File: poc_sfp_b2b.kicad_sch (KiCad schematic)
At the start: 16 parts

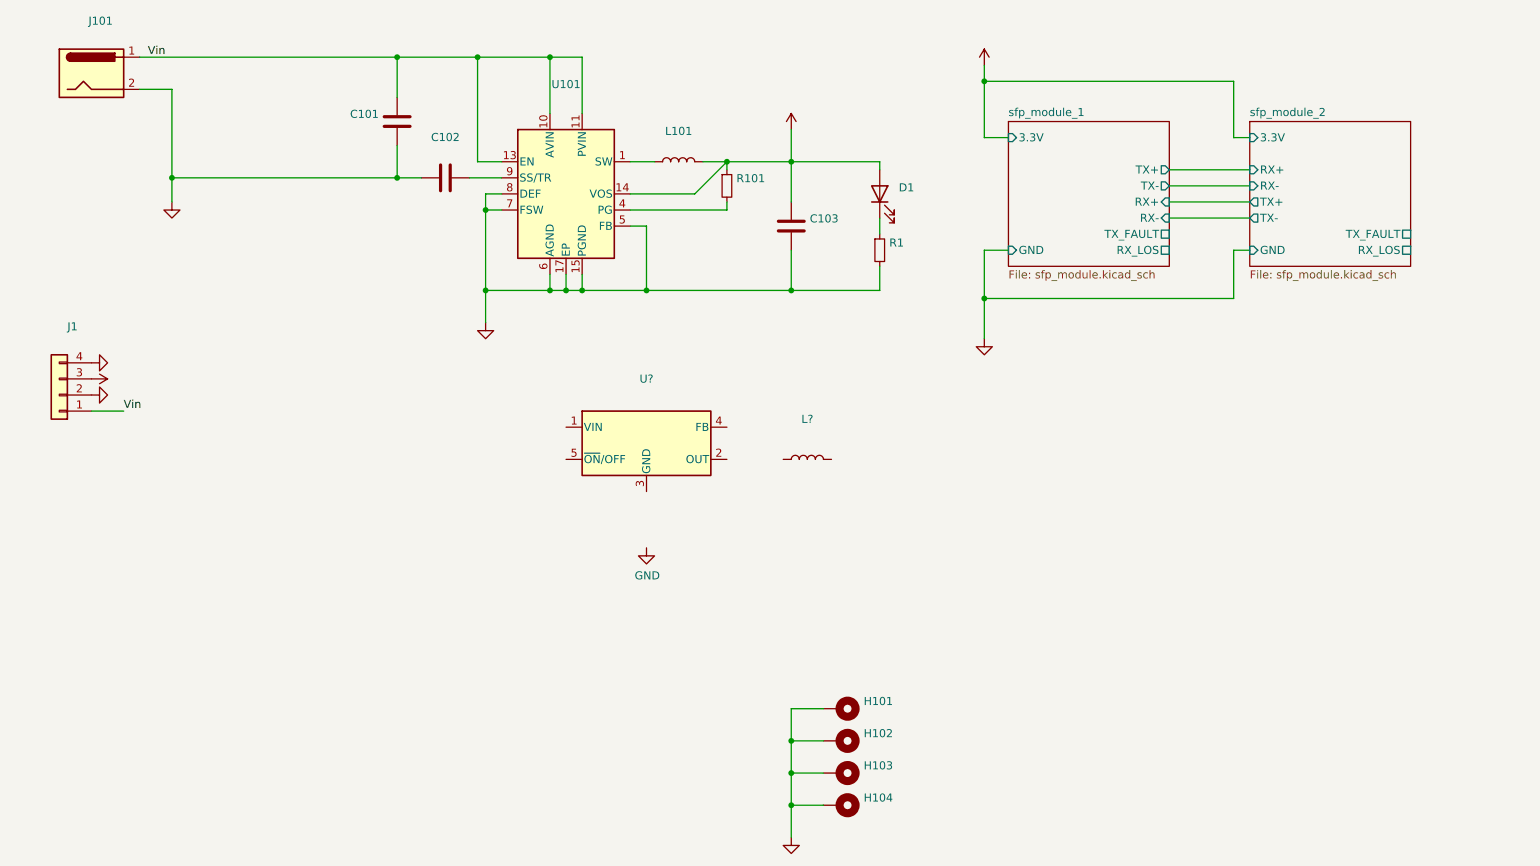
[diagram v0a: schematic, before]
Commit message: Replaced Mouser with LCSC Components
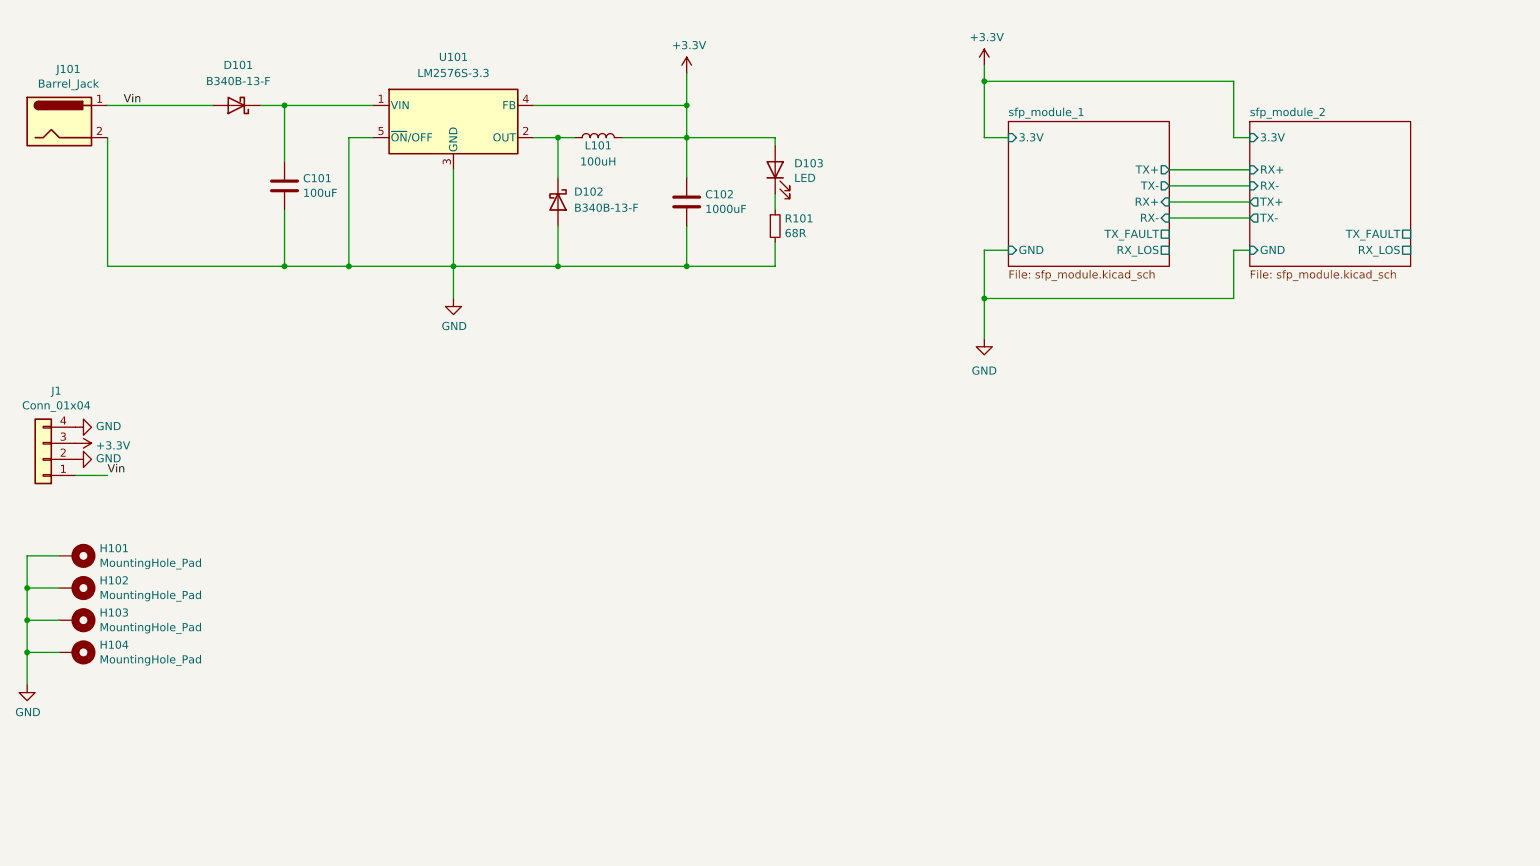
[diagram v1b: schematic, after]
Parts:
- removed C102: (no value), symbol Device:C
- removed L101: (no value), symbol Device:L
- removed R101: (no value), symbol Device:R_Small
- removed U101: (no value), symbol Regulator_Switching:TPS62142
- added D101, D102: B340B-13-F, Diode_SMD:D_SMB, symbol Device:D_Schottky
- C101: value (none) -> 100uF; footprint (none) -> Capacitor_SMD:CP_Elec_10x10; LCSC (none) -> C249838; Mouser Link https://www.mouser.de/ProductDetail/Samsung-Electro-Mechani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 -> (none); Mouser Part Number 187-CL32A106KAULNNE -> (none); Part Number CL32A106KAULNNE -> (none)
- C102: renamed from C103; value (none) -> 1000uF; footprint (none) -> Capacitor_SMD:CP_Elec_10x10; LCSC Part Number (none) -> C249844; Mouser Link https://www.mouser.de/ProductDetail/Samsung-Electro-Mechani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 -> (none); Mouser Part Number 187-CL21A226KQCLRNC -> (none); Part Number CL21A226KQCLRNC -> (none)
- D103: renamed from D1; value (none) -> LED; footprint (none) -> LED_THT:LED_D3.0mm_Horizontal_O1.27mm_Z2.0mm; LCSC Part Number (none) -> C181864
- H101, H102, H103, H104: value (none) -> MountingHole_Pad
- J1: value (none) -> Conn_01x04; footprint (none) -> Connector_PinHeader_2.54mm:PinHeader_1x04_P2.54mm_Vertical
- J101: value (none) -> Barrel_Jack; footprint (none) -> Connector_BarrelJack:BarrelJack_Horizontal; LCSC Part Number (none) -> C194407; Mouser Link https://www.mouser.de/ProductDetail/Gravitech/CON-SOCJ-2155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 -> (none); Mouser Part Number 992-CON-SOCJ-2155 -> (none); Part Number CON-SOCJ-2155 -> (none)
- L101: renamed from L?; value (none) -> 100uH; footprint (none) -> Inductor_SMD:L_10.4x10.4_H4.8; LCSC Part Number (none) -> C2875675
- R101: renamed from R1; value (none) -> 68R; footprint (none) -> Resistor_SMD:R_0805_2012Metric; LCSC Part Number (none) -> C474219
- U101: renamed from U?; value (none) -> LM2576S-3.3; footprint (none) -> Package_TO_SOT_SMD:TO-263-5_TabPin3; LCSC Part Number (none) -> C91093
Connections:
- net +3V3: now also L101.2, U101.4 (FB)
- net GND: now also U101.3 (GND), U101.5 (~{ON}/OFF), D102.2 (A)
- net Vin: now also D101.2 (A); no longer C101.1
- net at L101.1: now also U101.2 (OUT), D102.1 (K)
- net at U101.1 (VIN): now also C101.1, D101.1 (K)
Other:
- moved on the sheet: C102, D103, H101, H102, H103, H104, J1, J101, L101, R101, U101

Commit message: Added I2C pins
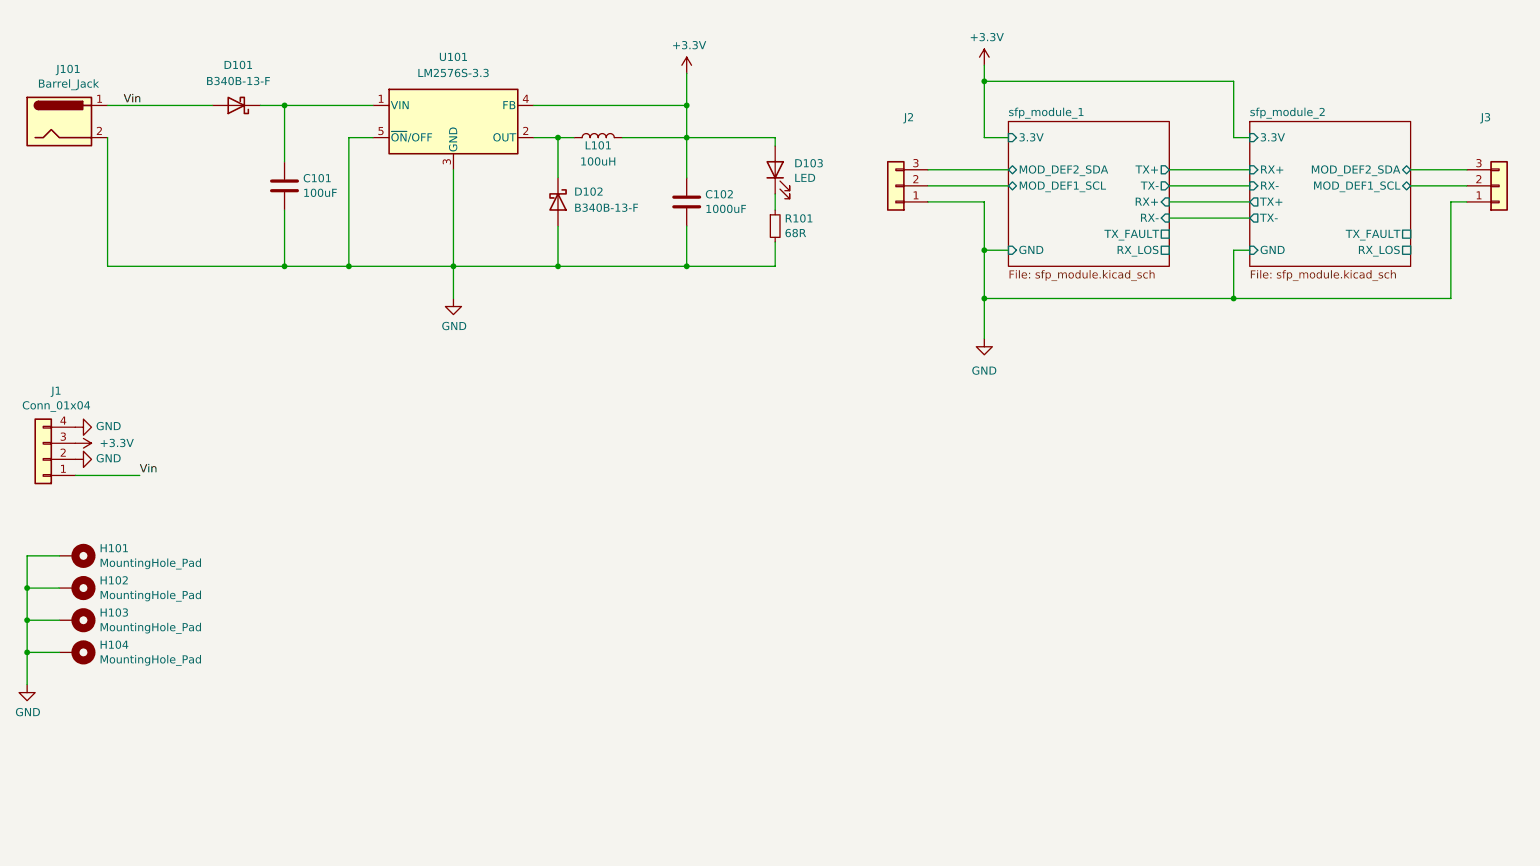
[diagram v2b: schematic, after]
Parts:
- added J2, J3: (no value), symbol Connector_Generic:Conn_01x03
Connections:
- net GND: now also J2.1 (Pin_1), J3.1 (Pin_1)
- new net sfp_module_1/MOD_DEF1_SCL: J2.2 (Pin_2)
- new net sfp_module_1/MOD_DEF2_SDA: J2.3 (Pin_3)
- new net sfp_module_2/MOD_DEF1_SCL: J3.2 (Pin_2)
- new net sfp_module_2/MOD_DEF2_SDA: J3.3 (Pin_3)
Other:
- sheet sfp_module_1 ports: added MOD_DEF1_SCL, MOD_DEF2_SDA; removed none
- sheet sfp_module_2 ports: added MOD_DEF1_SCL, MOD_DEF2_SDA; removed none
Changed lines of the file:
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@@
   (junction (at 127 101.6) (diameter 0) (color 0 0 0 0)
   )
+  (junction (at 173.99 99.06) (diameter 0) (color 0 0 0 0)
+  )
   (junction (at 173.99 72.39) (diameter 0) (color 0 0 0 0)
   )
   (junction (at 106.68 81.28) (diameter 0) (color 0 0 0 0)
   )
+  (junction (at 213.36 106.68) (diameter 0) (color 0 0 0 0)
+  )
   (junction (at 173.99 106.68) (diameter 0) (color 0 0 0 0)
   )
@@
     (stroke (width 0) (type default) (color 0 0 0 0))
   )
+  (wire (pts (xy 213.36 106.68) (xy 247.65 106.68))
+    (stroke (width 0) (type default) (color 0 0 0 0))
+  )
   (wire (pts (xy 173.99 106.68) (xy 173.99 99.06))
     (stroke (width 0) (type default) (color 0 0 0 0))
@@
     (stroke (width 0) (type default) (color 0 0 0 0))
   )
+  (wire (pts (xy 247.65 91.44) (xy 250.19 91.44))
+    (stroke (width 0) (type default) (color 0 0 0 0))
+  )
   (wire (pts (xy 27.94 152.4) (xy 22.86 152.4))
     (stroke (width 0) (type default) (color 0 0 0 0))
@@
     (stroke (width 0) (type default) (color 0 0 0 0))
   )
+  (wire (pts (xy 241.3 86.36) (xy 250.19 86.36))
+    (stroke (width 0) (type default) (color 0 0 0 0))
+  )
   (wire (pts (xy 203.2 91.44) (xy 215.9 91.44))
     (stroke (width 0) (type default) (color 0 0 0 0))
@@
     (stroke (width 0) (type default) (color 0 0 0 0))
   )
-  (wire (pts (xy 30.48 134.62) (xy 35.56 134.62))
+  (wire (pts (xy 30.48 134.62) (xy 40.64 134.62))
     (stroke (width 0) (type default) (color 0 0 0 0))
   )
@@
     (stroke (width 0) (type default) (color 0 0 0 0))
   )
+  (wire (pts (xy 165.1 91.44) (xy 173.99 91.44))
+    (stroke (width 0) (type default) (color 0 0 0 0))
+  )
   (wire (pts (xy 35.56 76.2) (xy 52.07 76.2))
     (stroke (width 0) (type default) (color 0 0 0 0))
@@
     (stroke (width 0) (type default) (color 0 0 0 0))
   )
+  (wire (pts (xy 165.1 88.9) (xy 177.8 88.9))
+    (stroke (width 0) (type default) (color 0 0 0 0))
+  )
   (wire (pts (xy 35.56 101.6) (xy 63.5 101.6))
     (stroke (width 0) (type default) (color 0 0 0 0))
   )
+  (wire (pts (xy 247.65 106.68) (xy 247.65 91.44))
+    (stroke (width 0) (type default) (color 0 0 0 0))
+  )
+  (wire (pts (xy 165.1 86.36) (xy 177.8 86.36))
+    (stroke (width 0) (type default) (color 0 0 0 0))
+  )
   (wire (pts (xy 77.47 81.28) (xy 73.66 81.28))
     (stroke (width 0) (type default) (color 0 0 0 0))
@@
     (stroke (width 0) (type default) (color 0 0 0 0))
   )
+  (wire (pts (xy 173.99 91.44) (xy 173.99 99.06))
+    (stroke (width 0) (type default) (color 0 0 0 0))
+  )
   (wire (pts (xy 173.99 69.85) (xy 173.99 72.39))
     (stroke (width 0) (type default) (color 0 0 0 0))
@@
     (stroke (width 0) (type default) (color 0 0 0 0))
   )
+  (wire (pts (xy 241.3 88.9) (xy 250.19 88.9))
+    (stroke (width 0) (type default) (color 0 0 0 0))
+  )
   (wire (pts (xy 22.86 147.32) (xy 27.94 147.32))
     (stroke (width 0) (type default) (color 0 0 0 0))
   )
-  (label "Vin" (at 35.56 134.62 0)
+  (label "Vin" (at 40.64 134.62 0)
     (effects (font (size 1.27 1.27)) (justify left bottom))
   )
@@
       (effects (font (size 1.27 1.27)) hide)
     )
-    (property "Value" "+3.3V" (id 1) (at 33.7312 129.921 90)
+    (property "Value" "+3.3V" (id 1) (at 34.29 129.54 90)
       (effects (font (size 1.27 1.27)) (justify left))
     )
@@
     )
     (pin "1")
+  )
+  (symbol (lib_id "Connector_Generic:Conn_01x03") (at 255.27 88.9 0) (mirror x) (unit 1)
+    (in_bom yes) (on_board yes)
+    (property "Reference" "J3" (id 0) (at 253.1872 78.105 0))
+    (property "Value" "" (id 1) (at 253.1872 80.4164 0))
+    (property "Footprint" "" (id 2) (at 255.27 88.9 0)
+      (effects (font (size 1.27 1.27)) hide)
+    )
+    (property "Datasheet" "~" (id 3) (at 255.27 88.9 0)
+      (effects (font (size 1.27 1.27)) hide)
+    )
+    (pin "1")
+    (pin "2")
+    (pin "3")
   )
   (symbol (lib_id "Device:C") (at 63.5 88.9 0) (unit 1)
@@
     (pin "1")
     (pin "2")
+  )
+  (symbol (lib_id "Connector_Generic:Conn_01x03") (at 160.02 88.9 180) (unit 1)
+    (in_bom yes) (on_board yes)
+    (property "Reference" "J2" (id 0) (at 162.1028 78.105 0))
+    (property "Value" "" (id 1) (at 162.1028 80.4164 0))
+    (property "Footprint" "" (id 2) (at 160.02 88.9 0)
+      (effects (font (size 1.27 1.27)) hide)
+    )
+    (property "Datasheet" "~" (id 3) (at 160.02 88.9 0)
+      (effects (font (size 1.27 1.27)) hide)
+    )
+    (pin "1")
+    (pin "2")
+    (pin "3")
   )
   (symbol (lib_id "Device:L") (at 113.03 81.28 90) (unit 1)
@@
       (effects (font (size 1.27 1.27)) (justify right))
     )
+    (pin "MOD_DEF2_SDA" bidirectional (at 241.3 86.36 0)
+      (effects (font (size 1.27 1.27)) (justify right))
+    )
+    (pin "MOD_DEF1_SCL" bidirectional (at 241.3 88.9 0)
+      (effects (font (size 1.27 1.27)) (justify right))
+    )
   )
   (sheet (at 177.8 78.74) (size 25.4 22.86) (fields_autoplaced)
@@
       (effects (font (size 1.27 1.27)) (justify right))
     )
+    (pin "MOD_DEF2_SDA" bidirectional (at 177.8 86.36 180)
+      (effects (font (size 1.27 1.27)) (justify left))
+    )
+    (pin "MOD_DEF1_SCL" bidirectional (at 177.8 88.9 180)
+      (effects (font (size 1.27 1.27)) (justify left))
+    )
   )
   (sheet_instances
@@
       (reference "J1") (unit 1) (value "Conn_01x04") (footprint "Connector_PinHeader_2.54mm:PinHeader_1x04_P2.54mm_Vertical")
     )
+    (path "/99f80a62-5038-4c47-a363-1656749f1df3"
+      (reference "J2") (unit 1) (value "Conn_01x03") (footprint "Connector_PinHeader_2.54mm:PinHeader_1x03_P2.54mm_Vertical")
+    )
+    (path "/7b8c43d0-e4a7-460c-bf6b-f0068724243b"
+      (reference "J3") (unit 1) (value "Conn_01x03") (footprint "Connector_PinHeader_2.54mm:PinHeader_1x03_P2.54mm_Vertical")
+    )
     (path "/00000000-0000-0000-0000-00005f4b88ce"
       (reference "J101") (unit 1) (value "Barrel_Jack") (footprint "Connector_BarrelJack:BarrelJack_Horizontal")
@@
     )
     (path "/00000000-0000-0000-0000-00005f4938c1/00000000-0000-0000-0000-00005f43569f"
-      (reference "R201") (unit 1) (value "10k") (footprint "Resistor_SMD:R_0805_2012Metric")
+      (reference "R201") (unit 1) (value "4.7k") (footprint "Resistor_SMD:R_0805_2012Metric")
     )
     (path "/00000000-0000-0000-0000-00005f4938c1/f14a57bf-7341-40f9-af74-347d093bc063"
-      (reference "R202") (unit 1) (value "10k") (footprint "Resistor_SMD:R_0805_2012Metric")
+      (reference "R202") (unit 1) (value "4.7k") (footprint "Resistor_SMD:R_0805_2012Metric")
     )
     (path "/00000000-0000-0000-0000-00005f4938c1/cbd46e20-52f0-4524-a92e-be7057481d7a"
-      (reference "R203") (unit 1) (value "10k") (footprint "Resistor_SMD:R_0805_2012Metric")
+      (reference "R203") (unit 1) (value "4.7k") (footprint "Resistor_SMD:R_0805_2012Metric")
     )
     (path "/00000000-0000-0000-0000-00005f4938c1/26d84874-cb74-4ac1-91ba-888941489f95"
-      (reference "R204") (unit 1) (value "10k") (footprint "Resistor_SMD:R_0805_2012Metric")
+      (reference "R204") (unit 1) (value "4.7k") (footprint "Resistor_SMD:R_0805_2012Metric")
     )
     (path "/00000000-0000-0000-0000-00005f4938c1/e9e15c47-aa28-45c6-bc4d-fae357e2441b"
-      (reference "R205") (unit 1) (value "10k") (footprint "Resistor_SMD:R_0805_2012Metric")
+      (reference "R205") (unit 1) (value "4.7k") (footprint "Resistor_SMD:R_0805_2012Metric")
     )
     (path "/00000000-0000-0000-0000-00005f49d702/00000000-0000-0000-0000-00005f43569f"
-      (reference "R301") (unit 1) (value "10k") (footprint "Resistor_SMD:R_0805_2012Metric")
+      (reference "R301") (unit 1) (value "4.7k") (footprint "Resistor_SMD:R_0805_2012Metric")
     )
     (path "/00000000-0000-0000-0000-00005f49d702/f14a57bf-7341-40f9-af74-347d093bc063"
-      (reference "R302") (unit 1) (value "10k") (footprint "Resistor_SMD:R_0805_2012Metric")
+      (reference "R302") (unit 1) (value "4.7k") (footprint "Resistor_SMD:R_0805_2012Metric")
     )
     (path "/00000000-0000-0000-0000-00005f49d702/cbd46e20-52f0-4524-a92e-be7057481d7a"
-      (reference "R303") (unit 1) (value "10k") (footprint "Resistor_SMD:R_0805_2012Metric")
+      (reference "R303") (unit 1) (value "4.7k") (footprint "Resistor_SMD:R_0805_2012Metric")
     )
     (path "/00000000-0000-0000-0000-00005f49d702/26d84874-cb74-4ac1-91ba-888941489f95"
-      (reference "R304") (unit 1) (value "10k") (footprint "Resistor_SMD:R_0805_2012Metric")
+      (reference "R304") (unit 1) (value "4.7k") (footprint "Resistor_SMD:R_0805_2012Metric")
     )
     (path "/00000000-0000-0000-0000-00005f49d702/e9e15c47-aa28-45c6-bc4d-fae357e2441b"
-      (reference "R305") (unit 1) (value "10k") (footprint "Resistor_SMD:R_0805_2012Metric")
+      (reference "R305") (unit 1) (value "4.7k") (footprint "Resistor_SMD:R_0805_2012Metric")
     )
     (path "/abd54e8a-7c7f-4310-aa7b-4dad62df253b"

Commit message: WIP
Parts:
- C102: value 1000uF -> (none); footprint Capacitor_SMD:CP_Elec_10x10 -> (none); LCSC Part Number C249844 -> C176684
- J2, J3: value (none) -> Conn_01x03; footprint (none) -> Connector_PinHeader_2.54mm:PinHeader_1x03_P2.54mm_Vertical
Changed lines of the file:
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@@
       (effects (font (size 1.27 1.27)) (justify left))
     )
-    (property "Value" "1000uF" (id 1) (at 129.921 92.583 0)
-      (effects (font (size 1.27 1.27)) (justify left))
-    )
-    (property "Footprint" "Capacitor_SMD:CP_Elec_10x10" (id 2) (at 127.9652 95.25 0)
+    (property "Value" "" (id 1) (at 129.921 92.583 0)
+      (effects (font (size 1.27 1.27)) (justify left))
+    )
+    (property "Footprint" "" (id 2) (at 127.9652 95.25 0)
       (effects (font (size 1.27 1.27)) hide)
     )
@@
       (effects (font (size 1.27 1.27)) hide)
     )
-    (property "LCSC Part Number" "C249844" (id 6) (at 127 91.44 0)
+    (property "LCSC Part Number" "C176684" (id 6) (at 127 91.44 0)
       (effects (font (size 1.27 1.27)) hide)
     )
@@
     (in_bom yes) (on_board yes)
     (property "Reference" "J3" (id 0) (at 253.1872 78.105 0))
-    (property "Value" "" (id 1) (at 253.1872 80.4164 0))
-    (property "Footprint" "" (id 2) (at 255.27 88.9 0)
+    (property "Value" "Conn_01x03" (id 1) (at 253.1872 80.4164 0))
+    (property "Footprint" "Connector_PinHeader_2.54mm:PinHeader_1x03_P2.54mm_Vertical" (id 2) (at 255.27 88.9 0)
       (effects (font (size 1.27 1.27)) hide)
     )
@@
     (in_bom yes) (on_board yes)
     (property "Reference" "J2" (id 0) (at 162.1028 78.105 0))
-    (property "Value" "" (id 1) (at 162.1028 80.4164 0))
-    (property "Footprint" "" (id 2) (at 160.02 88.9 0)
+    (property "Value" "Conn_01x03" (id 1) (at 162.1028 80.4164 0))
+    (property "Footprint" "Connector_PinHeader_2.54mm:PinHeader_1x03_P2.54mm_Vertical" (id 2) (at 160.02 88.9 0)
       (effects (font (size 1.27 1.27)) hide)
     )
@@
     )
     (path "/00000000-0000-0000-0000-00005f4938c1/00000000-0000-0000-0000-00005f44119b"
-      (reference "L201") (unit 1) (value "1uH") (footprint "Inductor_SMD:L_0805_2012Metric")
+      (reference "L201") (unit 1) (value "1uH") (footprint "Inductor_SMD:L_1008_2520Metric")
     )
     (path "/00000000-0000-0000-0000-00005f4938c1/00000000-0000-0000-0000-00005f44a49f"
-      (reference "L202") (unit 1) (value "1uH") (footprint "Inductor_SMD:L_0805_2012Metric")
+      (reference "L202") (unit 1) (value "1uH") (footprint "Inductor_SMD:L_1008_2520Metric")
     )
     (path "/00000000-0000-0000-0000-00005f49d702/00000000-0000-0000-0000-00005f44119b"
-      (reference "L301") (unit 1) (value "1uH") (footprint "Inductor_SMD:L_0805_2012Metric")
+      (reference "L301") (unit 1) (value "1uH") (footprint "Inductor_SMD:L_1008_2520Metric")
     )
     (path "/00000000-0000-0000-0000-00005f49d702/00000000-0000-0000-0000-00005f44a49f"
-      (reference "L302") (unit 1) (value "1uH") (footprint "Inductor_SMD:L_0805_2012Metric")
+      (reference "L302") (unit 1) (value "1uH") (footprint "Inductor_SMD:L_1008_2520Metric")
     )
     (path "/00000000-0000-0000-0000-00005f4938c1/00000000-0000-0000-0000-00005fc9997e"
